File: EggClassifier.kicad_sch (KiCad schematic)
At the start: 0 parts

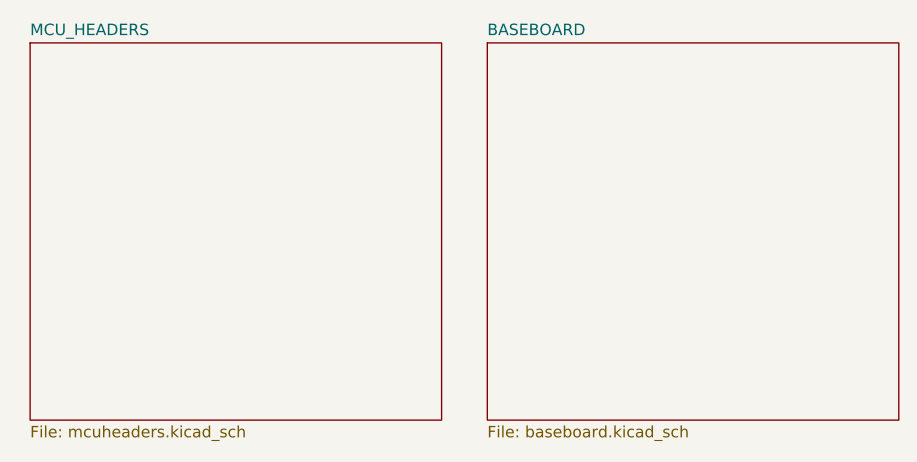
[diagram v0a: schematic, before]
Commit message: start of new board with STM32H743VIT6 included
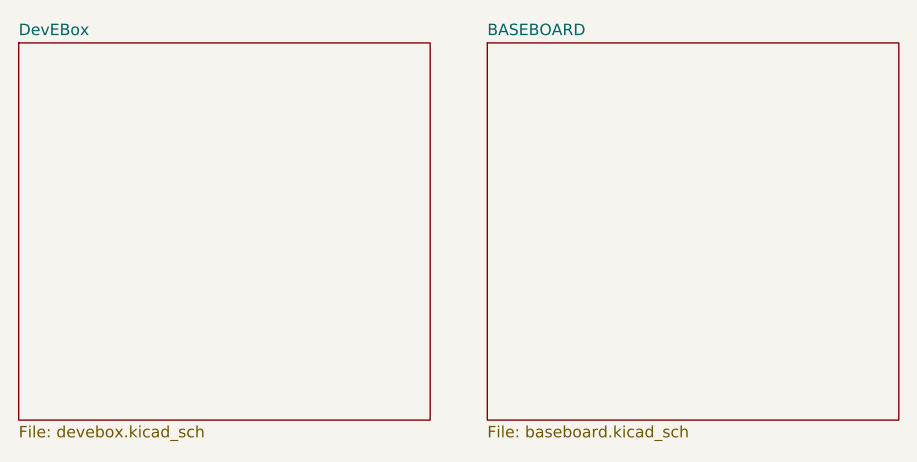
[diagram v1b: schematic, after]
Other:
- removed sheet MCU_HEADERS
- added sheet DevEBox (devebox.kicad_sch)
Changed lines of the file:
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@@
 	)
 	(sheet
-		(at 69.85 50.8)
+		(at 68.58 50.8)
 		(size 45.72 41.91)
 		(exclude_from_sim no)
@@
 			(color 0 0 0 0.0000)
 		)
-		(property "Sheetname" "MCU_HEADERS"
-			(at 69.85 50.0884 0)
+		(property "Sheetname" "DevEBox"
+			(at 68.58 50.0884 0)
 			(effects
 				(font
@@
 			)
 		)
-		(property "Sheetfile" "mcuheaders.kicad_sch"
-			(at 69.85 93.2946 0)
+		(property "Sheetfile" "devebox.kicad_sch"
+			(at 68.58 93.2946 0)
 			(effects
 				(font
@@
 			(project "EggClassifier"
 				(path "/1c72d2eb-7fb1-49fe-a026-e817f5a7ec43"
-					(page "2")
+					(page "4")
 				)
 			)
